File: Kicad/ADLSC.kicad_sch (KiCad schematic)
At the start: 52 parts, among them J1 Weidmueller 1824810000 or 176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, J2 Weidmueller 1824810000 or 176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, J3 Weidmueller 1824810000 or 176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, J4 Weidmueller 1824810000 or 176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, Q1 AOD442, Q2 MMBT2222, Q3 TSM160P02CS, Q4 TSM160P02CS, U1 74AHCT125D, U3 MAX809M

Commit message: progress
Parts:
- added H1, H2, H3, H4: MountingHole_Pad, MountingHole:MountingHole_3.2mm_M3_Pad_Via, symbol Mechanical:MountingHole_Pad
- added J5: Pmod host I2C, Connector_PinSocket_2.54mm-extra:PinSocket_1x06_P2.54mm_Horizontal, symbol Connector-extra:Pmod-host-i2c
- added J6: Pmod host SPI, Connector_PinSocket_2.54mm-extra:PinSocket_1x06_P2.54mm_Horizontal, symbol Connector-extra:Pmod-host-spi
- added R1, R16, R2, R3: 100R, Resistor_SMD:R_0805_2012Metric_Pad1.20x1.40mm_HandSolder, symbol Device:R
- A2: value ESP32-DevKitC -> ESP32-DevKitC + ESP32-WROVER-E
- C1: value 10uF -> 100n
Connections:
- net +3.3V: now also J5.6 (VCC), J6.6 (VCC)
- net +5V: now also U3.3 (VDD)
- net +5V_IN: no longer U3.3 (VDD)
- net CLK: now also A2.30 (SPI_CLK/IO18), R16.2; no longer J3.2 (Pin_2), R10.2
- net GND: now also H1.1, H2.1, H3.1, H4.1, J5.5 (GND), J6.5 (GND)
- net MOSI: now also A2.37 (SPI_MOSI/IO23), R2.2; no longer J3.1 (Pin_1), R9.2
- net SCL: now also J5.3 (SCL)
- net SDA: now also J5.4 (SDA)
- net CS0: now reaches A2.29 (SPI_CS0/BH/IO5)
- net CS0: now also R1.2
- net MISO: now reaches A2.31 (SPI_MISO/IO19)
- net MISO: now also R3.2
- net +5V_NEO1 renamed +5V_LED1
- net +5V_NEO2 renamed +5V_LED2
- net CLK_3V renamed DATA2_3V
- net MOSI_3V renamed DATA1_3V
- net NEO_ON renamed POWER_ON
- new net: J6.3 (MISO), R3.1
- new net: J6.1 (~{CS}), R1.1
- new net: J6.2 (MOSI), R2.1
- new net: J6.4 (SCK), R16.1
- new net DATA1: J3.1 (Pin_1), R9.2
- new net DATA2: J3.2 (Pin_2), R10.2
- no-connect marks 29 -> 27
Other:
- note added: "Feature creep connectors"
- note added: "LED data 3V3 to 5V level converter."
- note added: "LED power control."
- note removed: "Neopixel 3V3 to 5V level converter."
- note removed: "Neopixel power control."
- title: ADLSC -> ADLSC, Atoomnet's Digital Led String Controller
- moved on the sheet: C4, C6, C7, D10, D11, D12, D13, D14, D6, D7, D8, F1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

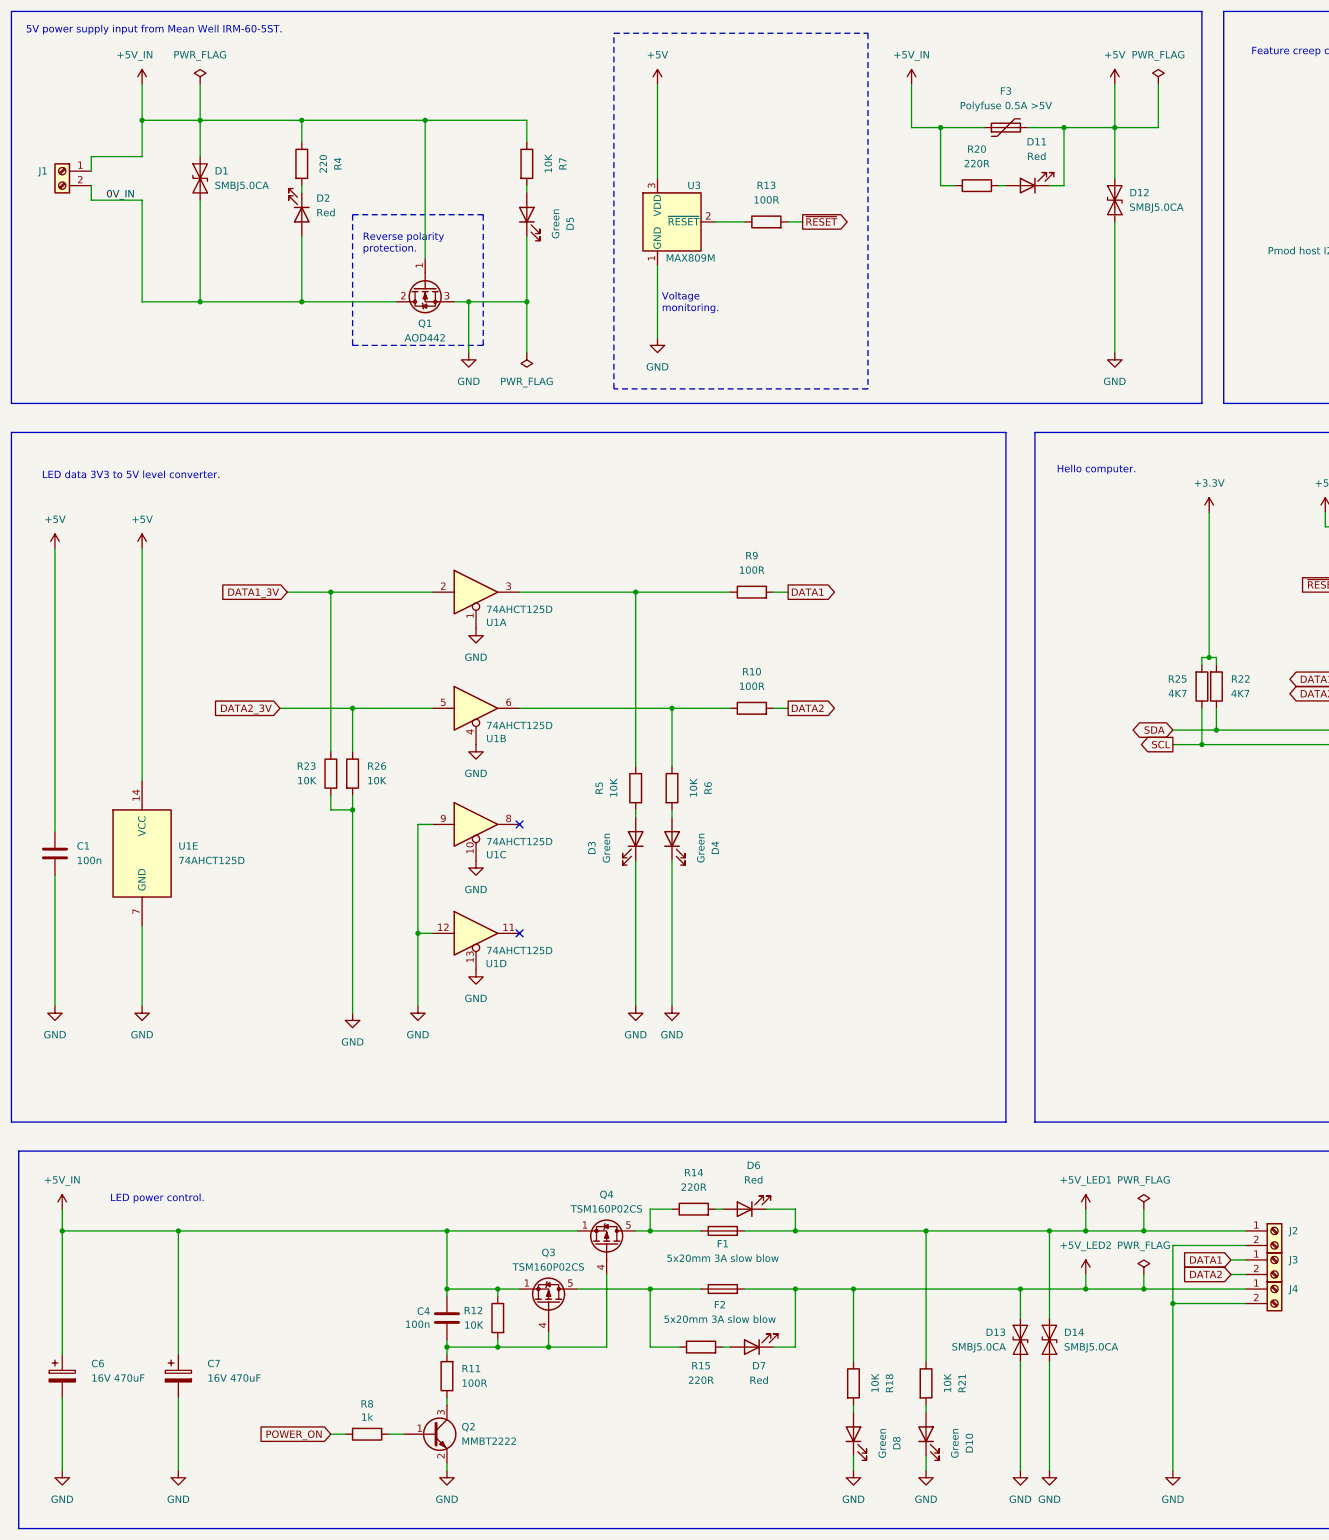
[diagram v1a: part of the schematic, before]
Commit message: Route PCB.
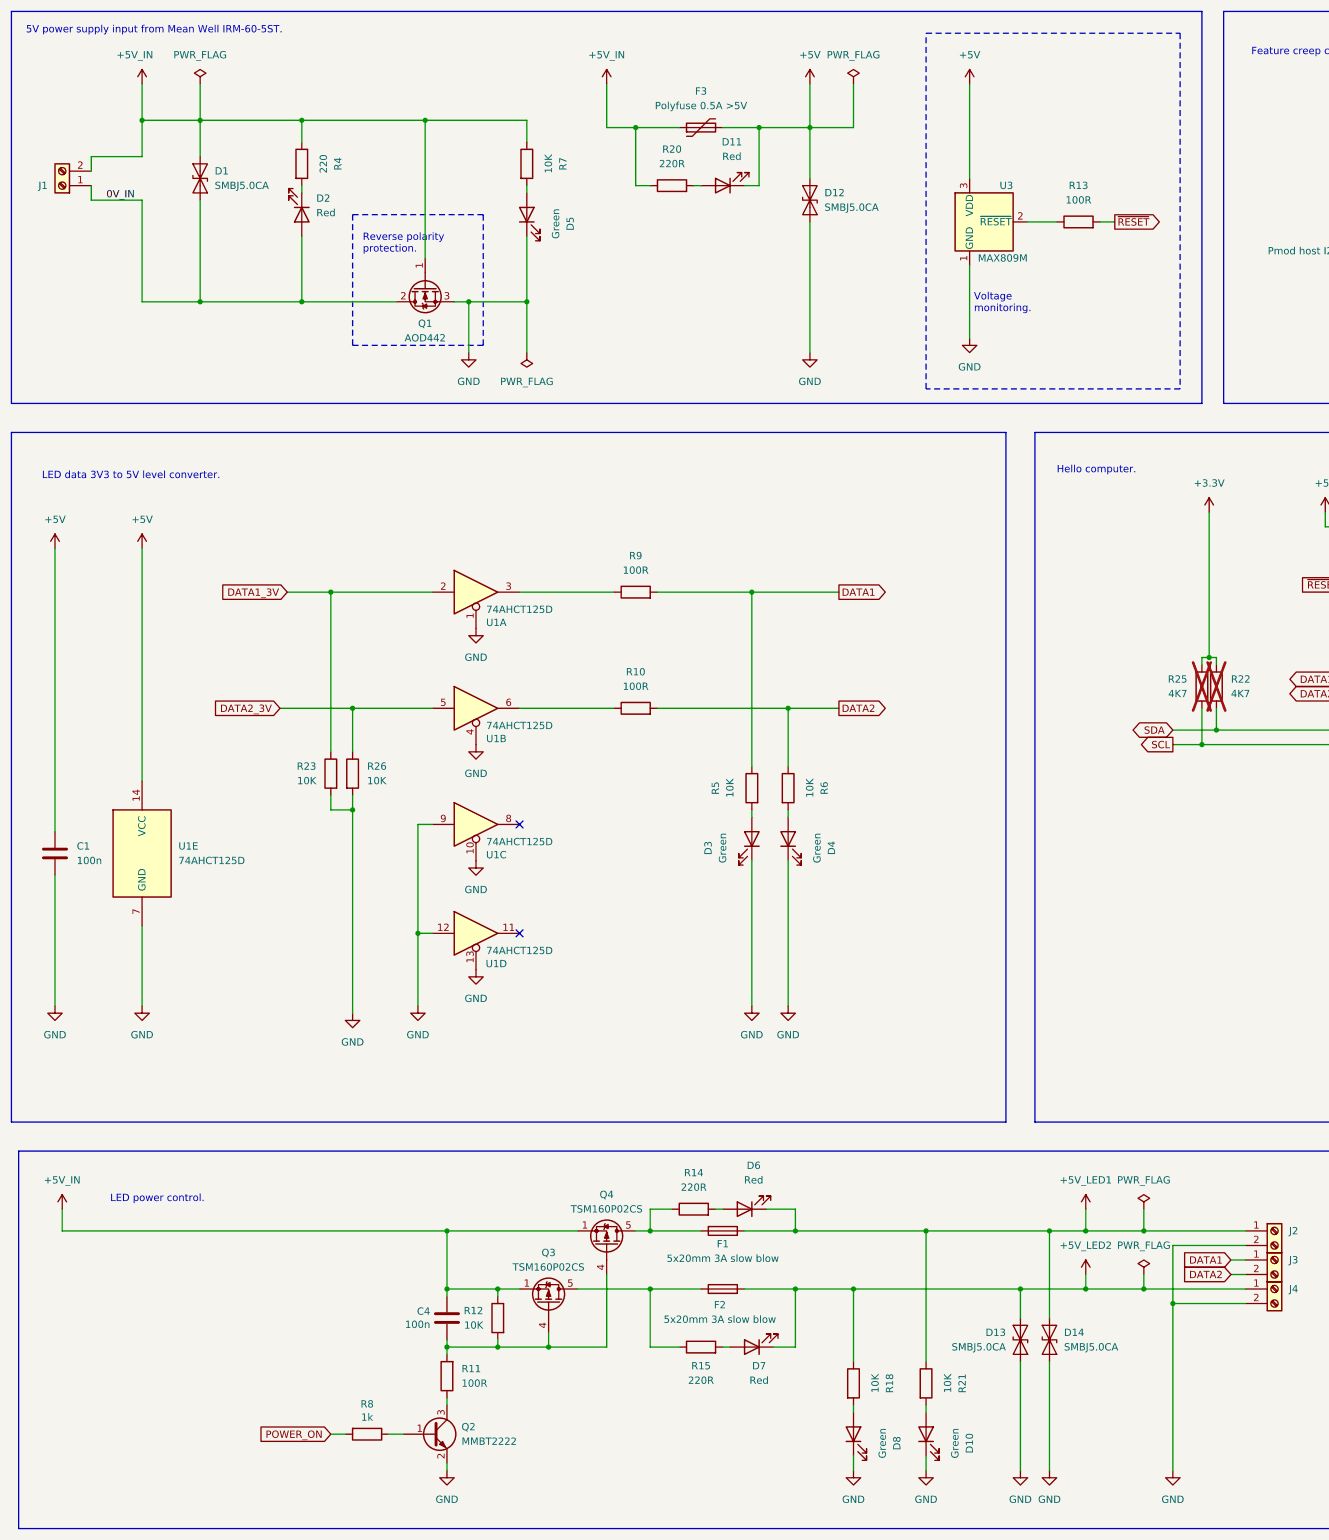
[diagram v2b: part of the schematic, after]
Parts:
- removed C6, C7: 16V 470uF, Capacitor_SMD:CP_Elec_10x10.5, symbol Device:C_Polarized
- D1, D12, D13, D14: footprint Diode_SMD:D_SMB -> Diode_SMD:D_SMA
- R22, R25: now not fitted
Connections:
- net +5V_IN: now also D1.1 (A1), J1.2 (Pin_2); no longer D1.2 (A2), J1.1 (Pin_1)
- net 0V_IN: now also D1.2 (A2), J1.1 (Pin_1); no longer D1.1 (A1), J1.2 (Pin_2)
- net DATA1: now also R5.1
- net DATA2: now also R6.1
- net at R10.1, U1.6: no longer R6.1
- net at R9.1, U1.3: no longer R5.1
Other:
- moved on the sheet: D1, D11, D12, D3, D4, F3, J1, R10, R13, R20, R5, R6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

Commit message: Finalize pcb. Add gerbers. Add more readme.
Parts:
- F2: renamed from F1; value 5x20mm 3A slow blow -> 2x fuseholder PCB clip with T3AL250V 5x20mm 3A slow blow fuse
- F3: renamed from F2; value 5x20mm 3A slow blow -> 2x fuseholder PCB clip with T3AL250V 5x20mm 3A slow blow fuse
- renumbered A2 to A1, C5 to C2, C4 to C3, D2 to D1, D4 to D10, D7 to D11, D8 to D12, D9 to D14, D5 to D2, D11 to D3, D1 to D4, D12 to D5, D10 to D6, D14 to D7, D6 to D8, D3 to D9, F3 to F1, J5 to J2, J2 to J3, J3 to J4, J6 to J5, J4 to J6, Q4 to Q2, Q2 to Q3, Q3 to Q4, R4 to R1, R21 to R10, R14 to R11, R9 to R12, R3 to R13, R26 to R14, R5 to R15, R10 to R16, R16 to R17, R6 to R18, R12 to R19, R7 to R2, R11 to R20, R8 to R21, R15 to R22, R18 to R23, R20 to R3, R25 to R4, R13 to R5, R22 to R6, R1 to R7, R23 to R8, R2 to R9, U3 to U1, U1 to U2
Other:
- moved on the sheet: C3, D11, D8, F2, F3, Q2, Q3, Q4, R11, R19, R20, R21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
